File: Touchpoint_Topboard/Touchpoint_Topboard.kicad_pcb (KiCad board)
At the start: 2 copper layers, 29 parts, among them J1 Conn_01x03, J2 Conn_01x03, J3 Conn_01x10, J4 EC10E1220501, Q1 NMOS, SW3 SW_SPST, U1 LT3750AEMS-TRPBF, U201 DA2032-AL

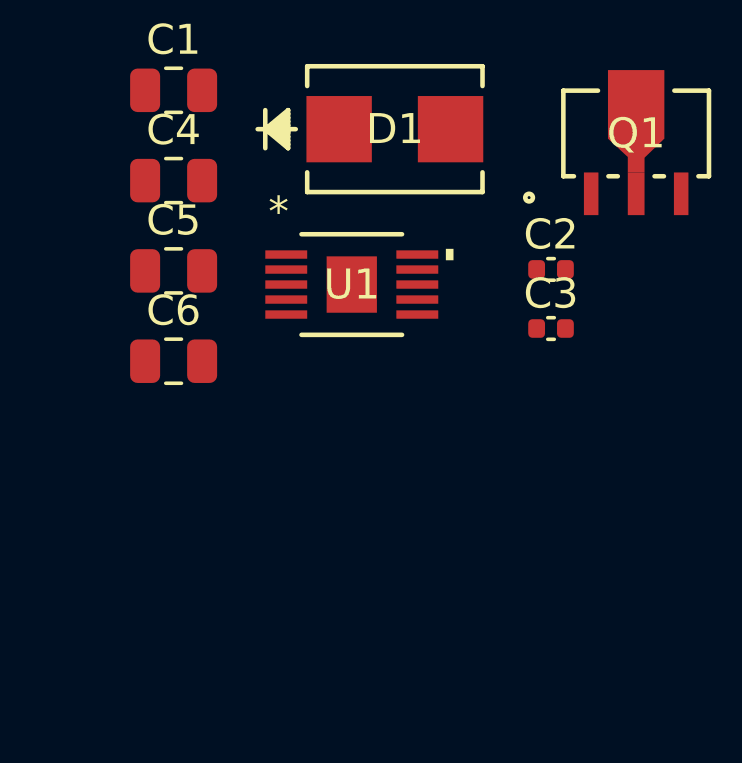
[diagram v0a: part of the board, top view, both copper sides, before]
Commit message: Actually finished assigning footprints in 3d models
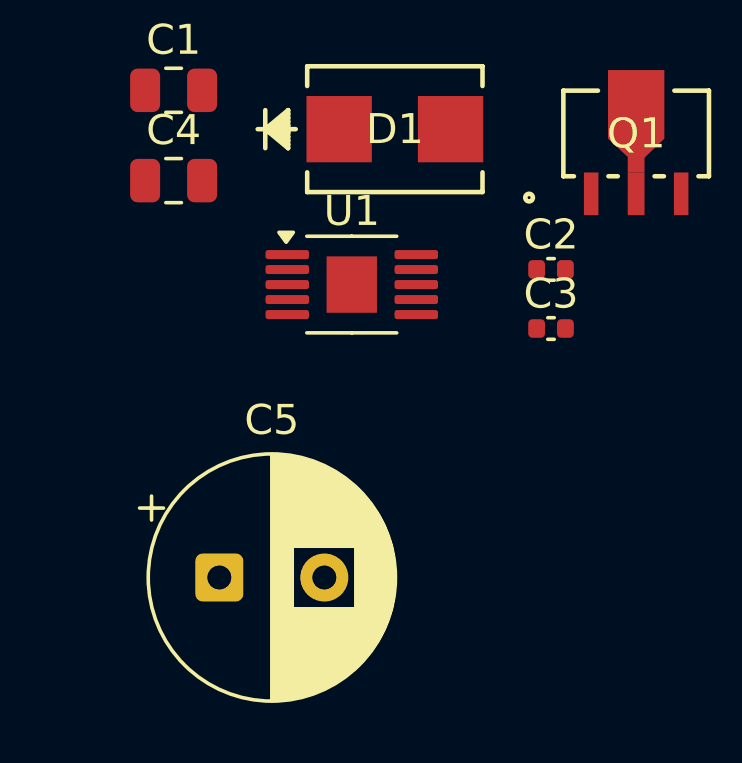
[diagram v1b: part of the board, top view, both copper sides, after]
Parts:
- removed C6: 22u, Capacitor_SMD:C_0805_2012Metric
- C5: value 22u -> 4.7u; footprint Capacitor_SMD:C_0805_2012Metric -> Capacitor_THT:CP_Radial_D8.0mm_P3.50mm
- U1: footprint Touchpoint:MSOP10_05-08-1664_ADI -> Package_SO:MSOP-10-1EP_3x3mm_P0.5mm_EP1.68x1.88mm
- moved C5 10.3 mm to (69.1, 90.4)
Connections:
- C5 pad 2: Net-(C5-Pad2) -> GND

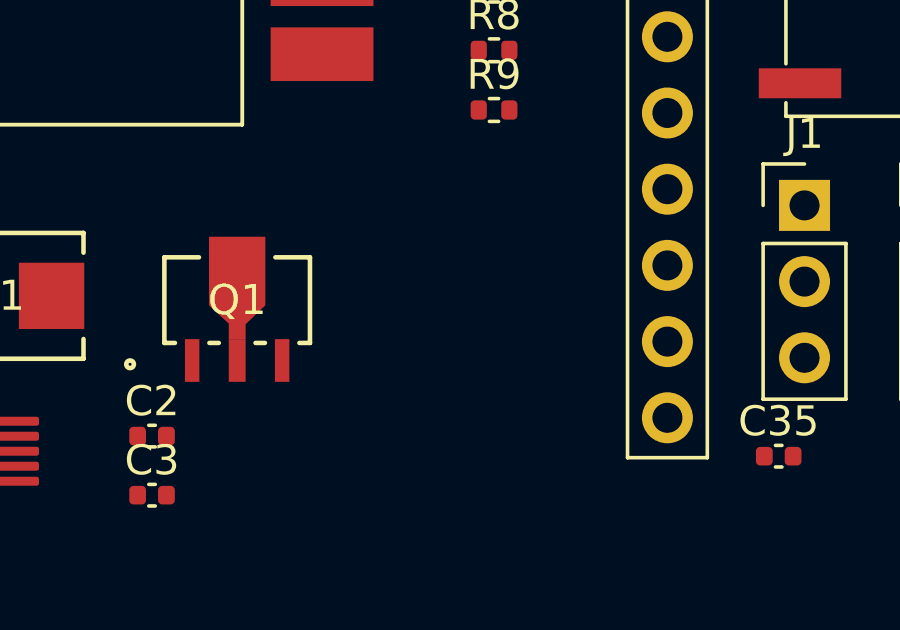
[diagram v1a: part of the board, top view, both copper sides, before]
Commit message: Added 5V regulator to flyback converter
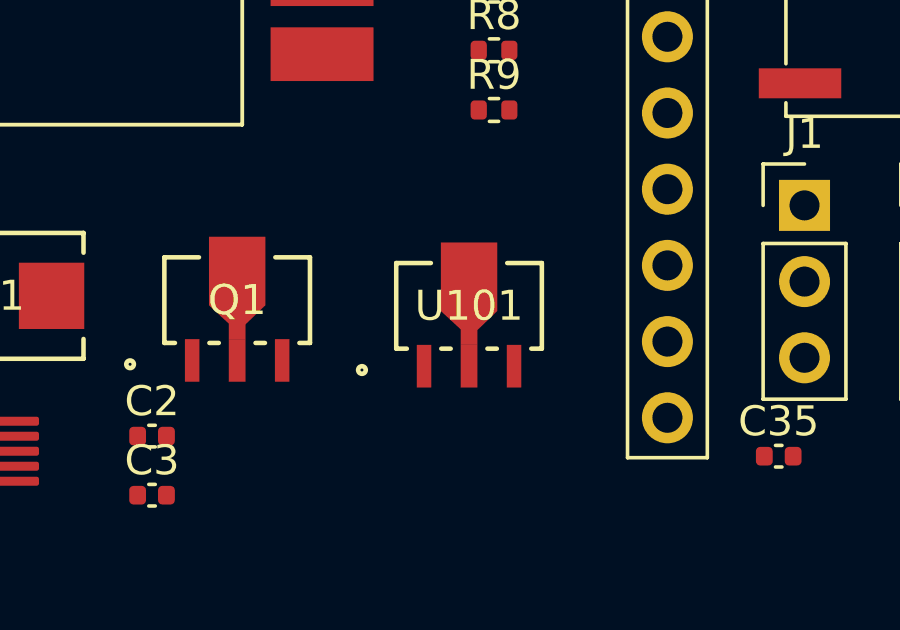
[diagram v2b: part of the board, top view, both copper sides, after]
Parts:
- added U101: AS78L05RTR-E1, Touchpoint:SOT-89_3MC_MCH, F.Cu at (90.7, 75.8)

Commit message: Added board outlines
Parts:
- moved J4 60.1 mm to (51.2, 28.5)
- moved J1 51.4 mm to (50.6, 68.5)
- moved SW3 49.9 mm to (68.4, 32.0)
- moved U201 45.5 mm to (39.0, 88.2)
- moved C1 43.7 mm to (34.0, 102.2)
- moved C2 43.7 mm to (46.6, 108.1)
- moved C3 43.7 mm to (46.6, 110.1)
- moved Q1 43.7 mm to (49.4, 103.6)
- moved U101 43.7 mm to (57.1, 103.8)
- moved U1 43.7 mm to (39.9, 108.6)
- moved C4 43.7 mm to (34.0, 105.2)
- moved D1 43.7 mm to (41.4, 103.4)
- moved J2 34.9 mm to (73.4, 83.5)
- moved C5 19.8 mm to (63.3, 109.4)
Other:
- board outline added: 51 x 96.4 mm
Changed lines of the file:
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@@
 		)
 		(property "Value" "300k"
-			(at 0 1.17 0)
+			(at -33.5707 29.1608 0)
 			(layer "F.Fab")
 			(effects
@@
 	(footprint "Touchpoint:SOT-89_3MC_MCH"
 		(layer "F.Cu")
-		(at 82.9707 75.598)
+		(at 49.4 103.5888)
 		(tags "DN3135N8-G ")
 		(property "Reference" "Q1"
@@
 	(footprint "Capacitor_SMD:C_0805_2012Metric"
 		(layer "F.Cu")
-		(at 67.5525 74.16)
+		(at 33.9818 102.1508)
 		(descr "Capacitor SMD 0805 (2012 Metric), square (rectangular) end terminal, IPC-7351 nominal, (Body size source: IPC-SM-782 page 76, https://www.pcb-3d.com/wordpress/wp-content/uploads/ipc-sm-782a_amendment_1_and_2.pdf, https://docs.google.com/spreadsheets/d/1BsfQQcO9C6DZCsRaXUlFlo91Tg2WpOkGARC1WS5S8t0/edit?usp=sharing), generated with kicad-footprint-generator")
 		(tags "capacitor")
@@
 	(footprint "Touchpoint:SW_SPST_EVQP0"
 		(layer "F.Cu")
-		(at 104.6125 66.37)
+		(at 68.4 32)
 		(descr "Light Touch Switch, https://industrial.panasonic.com/cdbs/www-data/pdf/ATK0000/ATK0000CE28.pdf")
 		(property "Reference" "SW3"
@@
 	(footprint "Touchpoint:SOT-89_3MC_MCH"
 		(layer "F.Cu")
-		(at 90.7 75.7888)
+		(at 57.1293 103.7796)
 		(tags "DN3135N8-G ")
 		(property "Reference" "U101"
@@
 	(footprint "Capacitor_THT:CP_Radial_D8.0mm_P3.50mm"
 		(layer "F.Cu")
-		(at 69.076041 90.4)
+		(at 63.347349 109.4)
 		(descr "CP, Radial series, Radial, pin pitch=3.50mm, diameter=8mm, height=12mm, Electrolytic Capacitor")
 		(tags "CP Radial series Radial pin pitch 3.50mm diameter 8mm height 12mm Electrolytic Capacitor")
@@
 	(footprint "Touchpoint:DA2032-AL"
 		(layer "F.Cu")
-		(at 75.64 61.15)
+		(at 39.04 88.25)
 		(property "Reference" "U201"
 			(at 0.17721 -1.634902 0)
@@
 	(footprint "Touchpoint:CONN03_EC10E_9P8X6P1_ALPS"
 		(layer "F.Cu")
-		(at 103.8867 57.375)
+		(at 51.183651 28.506911)
 		(tags "EC10E1220501 ")
 		(property "Reference" "J4"
@@
 	(footprint "Capacitor_SMD:C_0805_2012Metric"
 		(layer "F.Cu")
-		(at 67.5525 77.17)
+		(at 33.9818 105.1608)
 		(descr "Capacitor SMD 0805 (2012 Metric), square (rectangular) end terminal, IPC-7351 nominal, (Body size source: IPC-SM-782 page 76, https://www.pcb-3d.com/wordpress/wp-content/uploads/ipc-sm-782a_amendment_1_and_2.pdf, https://docs.google.com/spreadsheets/d/1BsfQQcO9C6DZCsRaXUlFlo91Tg2WpOkGARC1WS5S8t0/edit?usp=sharing), generated with kicad-footprint-generator")
 		(tags "capacitor")
@@
 	(footprint "Connector_PinHeader_2.54mm:PinHeader_1x03_P2.54mm_Vertical"
 		(layer "F.Cu")
-		(at 106.4725 72.44)
+		(at 73.4 83.46)
 		(descr "Through hole straight pin header, 1x03, 2.54mm pitch, single row")
 		(tags "Through hole pin header THT 1x03 2.54mm single row")
@@
 	(footprint "Connector_PinHeader_2.54mm:PinHeader_1x03_P2.54mm_Vertical"
 		(layer "F.Cu")
-		(at 101.8825 72.44)
+		(at 50.6 68.46)
 		(descr "Through hole straight pin header, 1x03, 2.54mm pitch, single row")
 		(tags "Through hole pin header THT 1x03 2.54mm single row")
@@
 	(footprint "Capacitor_SMD:C_0402_1005Metric"
 		(layer "F.Cu")
-		(at 80.1325 82.1)
+		(at 46.5618 110.0908)
 		(descr "Capacitor SMD 0402 (1005 Metric), square (rectangular) end terminal, IPC-7351 nominal, (Body size source: IPC-SM-782 page 76, https://www.pcb-3d.com/wordpress/wp-content/uploads/ipc-sm-782a_amendment_1_and_2.pdf), generated with kicad-footprint-generator")
 		(tags "capacitor")
@@
 	(footprint "Capacitor_SMD:C_0402_1005Metric"
 		(layer "F.Cu")
-		(at 80.1325 80.13)
+		(at 46.5618 108.1208)
 		(descr "Capacitor SMD 0402 (1005 Metric), square (rectangular) end terminal, IPC-7351 nominal, (Body size source: IPC-SM-782 page 76, https://www.pcb-3d.com/wordpress/wp-content/uploads/ipc-sm-782a_amendment_1_and_2.pdf), generated with kicad-footprint-generator")
 		(tags "capacitor")
@@
 	(footprint "Package_SO:MSOP-10-1EP_3x3mm_P0.5mm_EP1.68x1.88mm"
 		(layer "F.Cu")
-		(at 73.4906 80.6346)
+		(at 39.9199 108.6254)
 		(descr "MSOP, 10 Pin (https://www.analog.com/media/en/technical-documentation/data-sheets/3805fg.pdf#page=18), generated with kicad-footprint-generator ipc_gullwing_generator.py")
 		(tags "MSOP SO")
@@
 	(footprint "Touchpoint:SMB_DIO"
 		(layer "F.Cu")
-		(at 74.926701 75.4552)
+		(at 41.356001 103.446)
 		(tags "MURS160-13-F ")
 		(property "Reference" "D1"
@@
 			(polygon
 				(pts
-					(xy 72.182501 73.536) (xy 77.670901 73.536) (xy 77.670901 74.2994) (xy 72.182501 74.2994)
+					(xy 38.611801 101.5268) (xy 44.100201 101.5268) (xy 44.100201 102.2902) (xy 38.611801 102.2902)
 				)
 			)
@@
 			(polygon
 				(pts
-					(xy 72.182501 76.611) (xy 77.670901 76.611) (xy 77.670901 77.3744) (xy 72.182501 77.3744)
+					(xy 38.611801 104.6018) (xy 44.100201 104.6018) (xy 44.100201 105.3652) (xy 38.611801 105.3652)
 				)
 			)
@@
 			(polygon
 				(pts
-					(xy 74.210501 74.2994) (xy 75.642901 74.2994) (xy 75.642901 76.611) (xy 74.210501 76.611)
+					(xy 40.639801 102.2902) (xy 42.072201 102.2902) (xy 42.072201 104.6018) (xy 40.639801 104.6018)
 				)
 			)
@@
 		)
 	)
+	(gr_arc
+		(start 75.5 113.4)
+		(mid 74.62132 115.52132)
+		(end 72.5 116.4)
+		(stroke
+			(width 0.1)
+			(type default)
+		)
+		(layer "Edge.Cuts")
+	)
+	(gr_circle
+		(center 72.5 113.4)
+		(end 73.75 113.4)
+		(stroke
+			(width 0.1)
+			(type default)
+		)
+		(fill no)
+		(layer "Edge.Cuts")
+	)
+	(gr_line
+		(start 27.5 116.4)
+		(end 72.5 116.4)
+		(stroke
+			(width 0.1)
+			(type default)
+		)
+		(layer "Edge.Cuts")
+	)
+	(gr_line
+		(start 75.499999 26.6)
+		(end 75.5 26.6)
+		(stroke
+			(width 0.1)
+			(type default)
+		)
+		(layer "Edge.Cuts")
+	)
+	(gr_circle
+		(center 59.20062 82.397398)
+		(end 60.45062 82.397398)
+		(stroke
+			(width 0.1)
+			(type default)
+		)
+		(fill no)
+		(layer "Edge.Cuts")
+	)
+	(gr_line
+		(start 24.5 75.98863)
+		(end 24.5 113.4)
+		(stroke
+			(width 0.1)
+			(type default)
+		)
+		(layer "Edge.Cuts")
+	)
+	(gr_circle
+		(center 72.5 26.6)
+		(end 73.75 26.6)
+		(stroke
+			(width 0.1)
+			(type default)
+		)
+		(fill no)
+		(layer "Edge.Cuts")
+	)
+	(gr_arc
+		(start 27.5 116.4)
+		(mid 25.37868 115.52132)
+		(end 24.5 113.4)
+		(stroke
+			(width 0.1)
+			(type default)
+		)
+		(layer "Edge.Cuts")
+	)
+	(gr_arc
+		(start 45.774 20)
+		(mid 59.658169 20.930897)
+		(end 73.293799 23.706925)
+		(stroke
+			(width 0.1)
+			(type default)
+		)
+		(layer "Edge.Cuts")
+	)
+	(gr_arc
+		(start 73.293799 23.706925)
+		(mid 74.885518 24.780851)
+		(end 75.499999 26.6)
+		(stroke
+			(width 0.1)
+			(type default)
+		)
+		(layer "Edge.Cuts")
+	)
+	(gr_line
+		(start 75.5 113.4)
+		(end 75.5 26.6)
+		(stroke
+			(width 0.1)
+			(type default)
+		)
+		(layer "Edge.Cuts")
+	)
+	(gr_line
+		(start 45.774 20)
+		(end 45.774 68.393398)
+		(stroke
+			(width 0.1)
+			(type default)
+		)
+		(layer "Edge.Cuts")
+	)
+	(gr_line
+		(start 35.4635 68.393398)
+		(end 45.774 68.393398)
+		(stroke
+			(width 0.1)
+			(type default)
+		)
+		(layer "Edge.Cuts")
+	)
+	(gr_circle
+		(center 59.20062 39.643398)
+		(end 60.45062 39.643398)
+		(stroke
+			(width 0.1)
+			(type default)
+		)
+		(fill no)
+		(layer "Edge.Cuts")
+	)
+	(gr_circle
+		(center 27.5 113.4)
+		(end 28.75 113.4)
+		(stroke
+			(width 0.1)
+			(type default)
+		)
+		(fill no)
+		(layer "Edge.Cuts")
+	)
+	(gr_arc
+		(start 35.4635 68.393398)
+		(mid 31.264162 74.042139)
+		(end 24.5 75.98863)
+		(stroke
+			(width 0.1)
+			(type default)
+		)
+		(layer "Edge.Cuts")
+	)
+	(group ""
+		(members "2322282d-8d6a-4d79-8c77-49aa6208c43a" "24f87e23-3ff9-4e04-a972-c269bbe709e2"
+			"27bec6e0-dafe-41ac-9ab4-85c4c5ff396d" "2b12096e-a2bd-4cf2-8ef4-6ff4577989da"
+			"2dae6bfc-1a94-4488-b5da-6802de248a44" "31a26b90-32b9-4fcf-82ec-fa3d0d29ee33"
+			"3f9916ba-e04e-48a4-b817-dce3fe48c787" "442b3b1b-c8d5-45bd-b305-ba19b1cead49"
+			"527c5cb0-6c1d-438b-8e0c-61abb3739ad1" "7ae17eab-414c-4c64-8689-1388cb927a72"
+			"7e089082-d776-46e6-975f-da04b3b58d7d" "812a8e4f-dd63-47ab-8802-28c9f19f070c"
+			"c2937acc-ba5f-4dd4-957f-aa8acecdede2" "d8ca7931-3ce0-480a-bf00-a664ec0a2af7"
+			"e7c2a0f0-82da-45d5-8b19-5f7c0de0f928" "f92cfcab-3d6a-4df0-8618-4b0e10e9de2c"
+		)
+	)

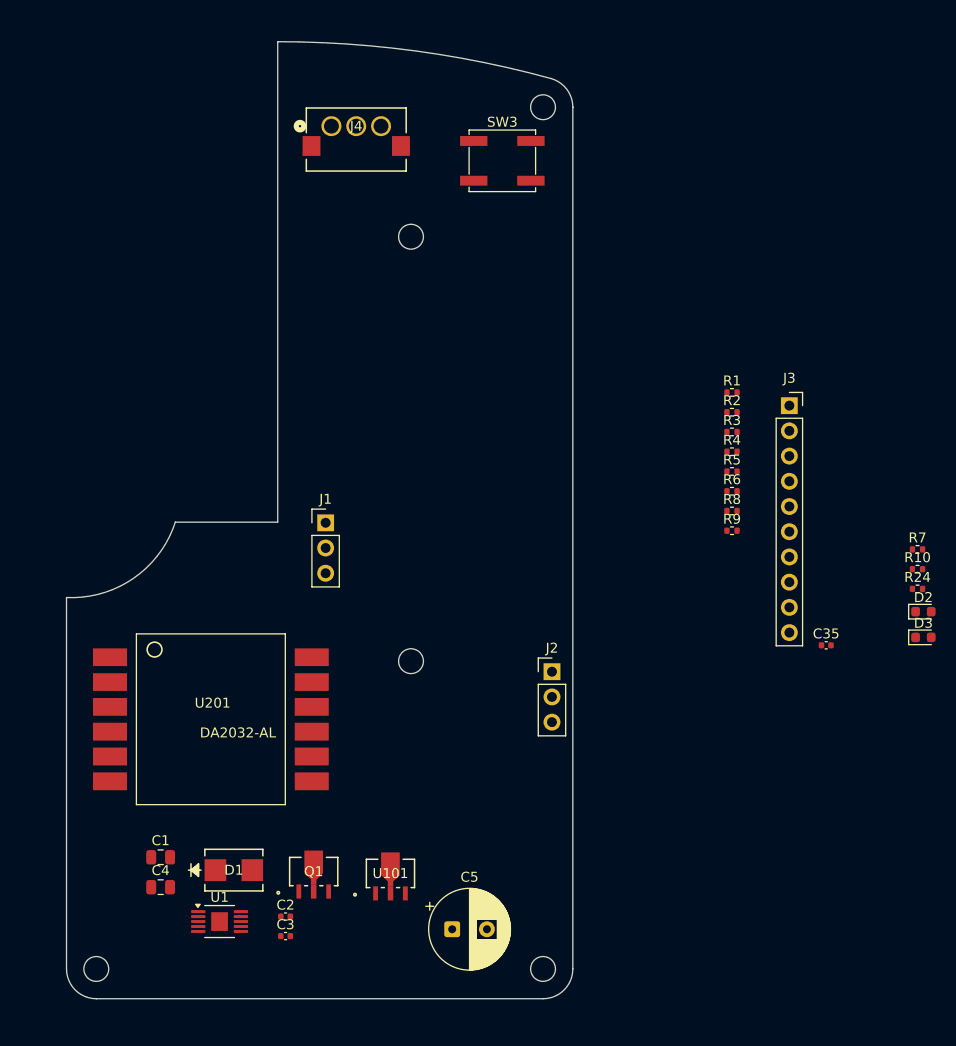
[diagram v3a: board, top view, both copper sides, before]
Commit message: Added servo mount outline
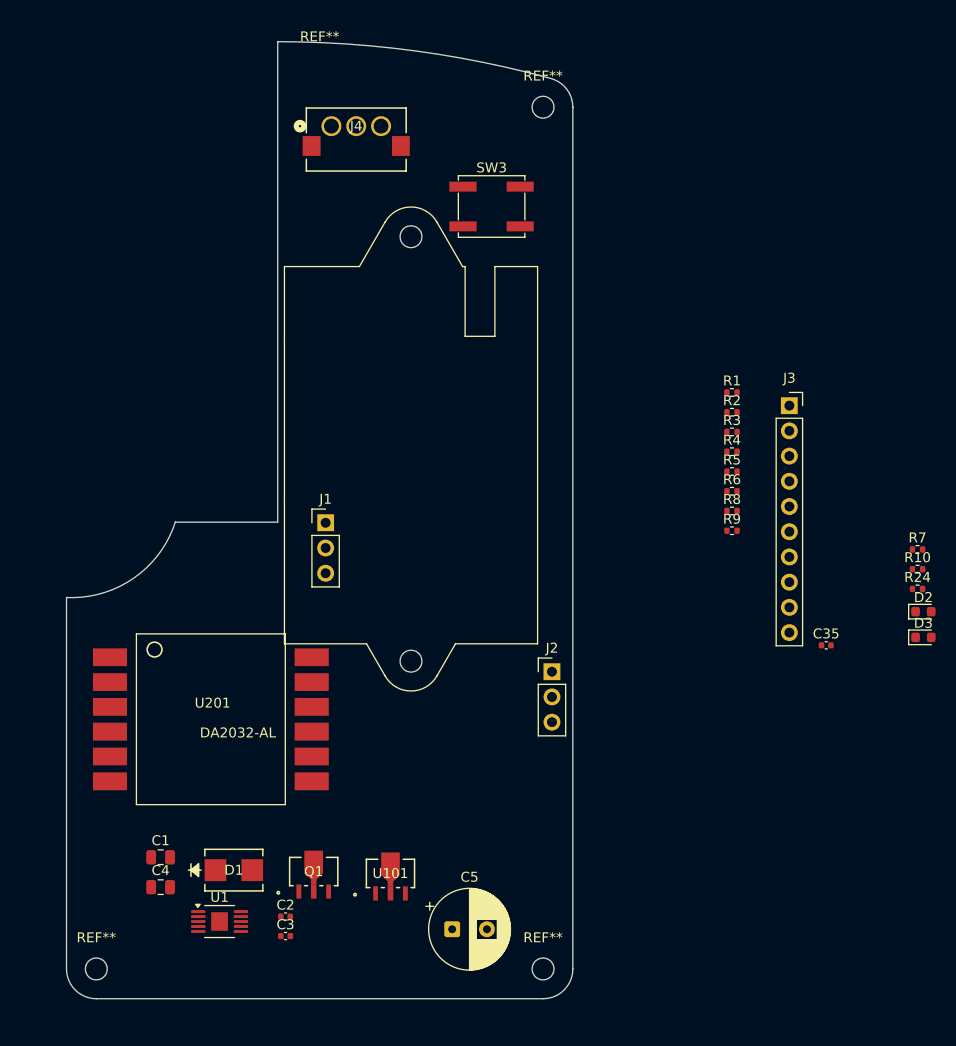
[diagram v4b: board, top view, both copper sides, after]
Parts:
- added REF**: MountingHole_2.2mm_M2, MountingHole:MountingHole_2.2mm_M2, F.Cu at (72.5, 113.4)
- added REF**: Servo_Mount, Touchpoint:Servo_Mount, F.Cu at (50.0, 20.0)
- added REF**: MountingHole_2.2mm_M2, MountingHole:MountingHole_2.2mm_M2, F.Cu at (27.5, 113.4)
- added REF**: MountingHole_2.2mm_M2, MountingHole:MountingHole_2.2mm_M2, F.Cu at (72.5, 26.6)
- moved SW3 4.73 mm to (67.3, 36.6)
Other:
- outline, holes or cut-outs redrawn

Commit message: Changed to jumper connector between boards
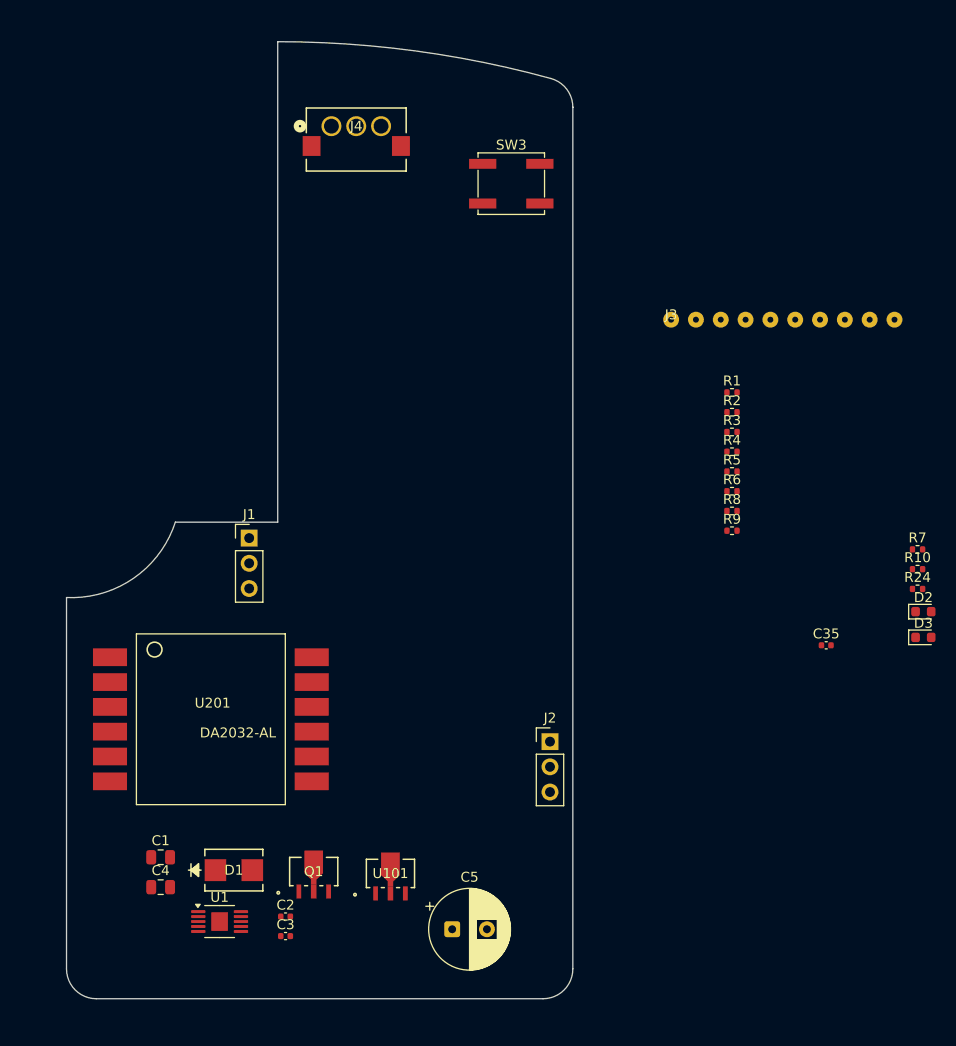
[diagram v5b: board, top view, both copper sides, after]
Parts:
- removed REF** (x3): MountingHole_2.2mm_M2, MountingHole:MountingHole_2.2mm_M2
- removed REF**: Servo_Mount, Touchpoint:Servo_Mount
- J3: footprint Connector_PinSocket_2.54mm:PinSocket_1x10_P2.54mm_Vertical -> Touchpoint:Jumper_Interface_10
- moved J3 14.7 mm to (85.4, 48.0)
- moved J1 7.85 mm to (42.9, 70.0)
- moved J2 7.04 mm to (73.2, 90.5)
- moved SW3 3.03 mm to (69.3, 34.3)
